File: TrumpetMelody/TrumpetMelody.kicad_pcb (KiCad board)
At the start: 2 copper layers, 76.2 x 68.6 mm, 81 parts, among them J1 USB_B_Micro, J2 Conn_01x05, J3 640456-3, J4 640456-3, SW1 SW_Push, U1 STM32F411RETx, U2 TLV62565DBVR, U3 MAX98357AETE_T, U4 MAX7375AXR805

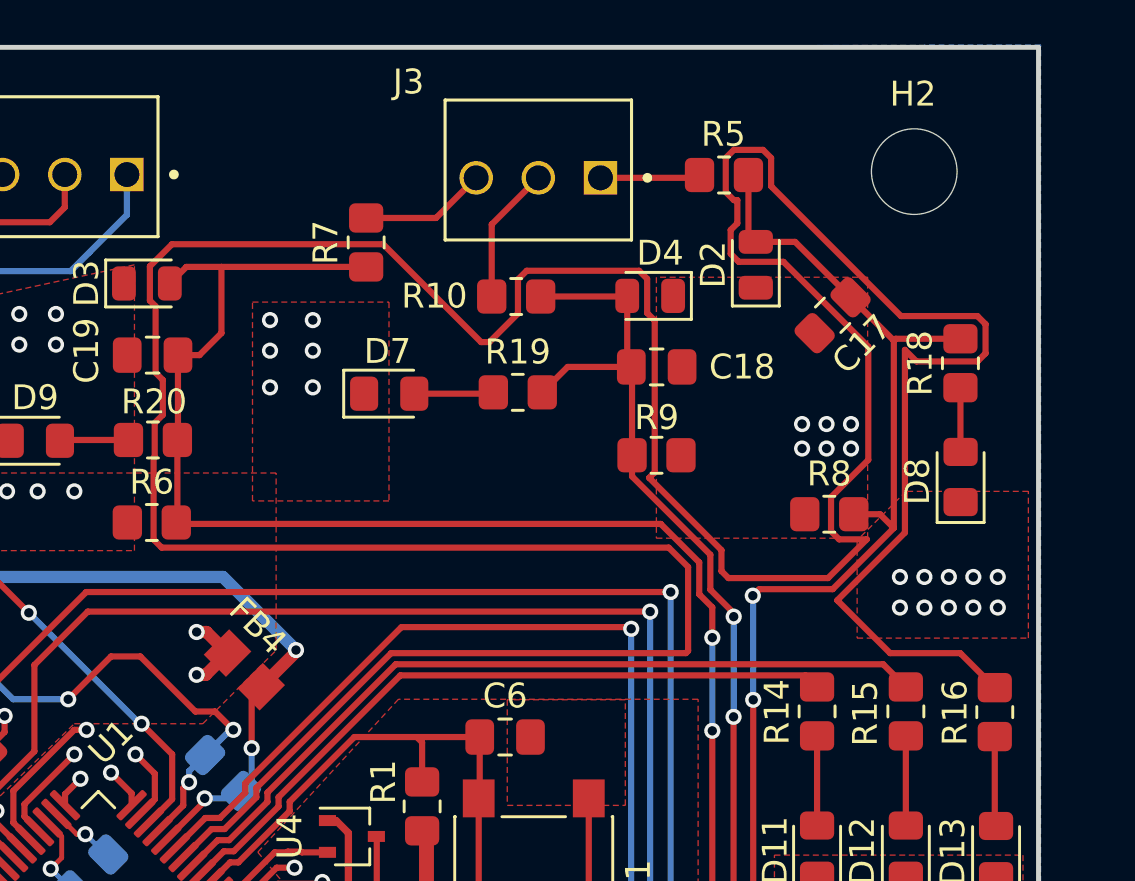
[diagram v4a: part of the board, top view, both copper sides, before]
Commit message: something autorouted and i just noticed it but now it is fixed
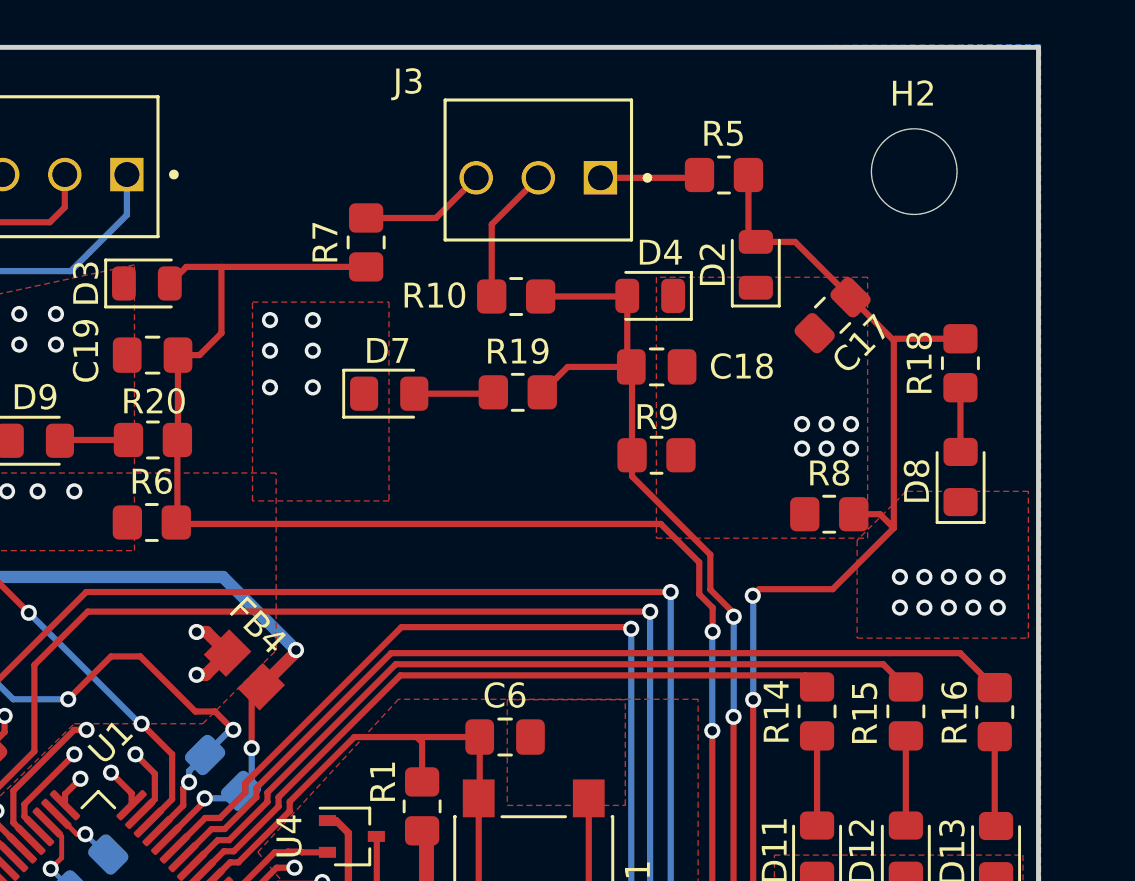
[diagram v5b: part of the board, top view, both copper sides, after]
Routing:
- net GPIO_LED2: track 166.0 -> 37.4 mm

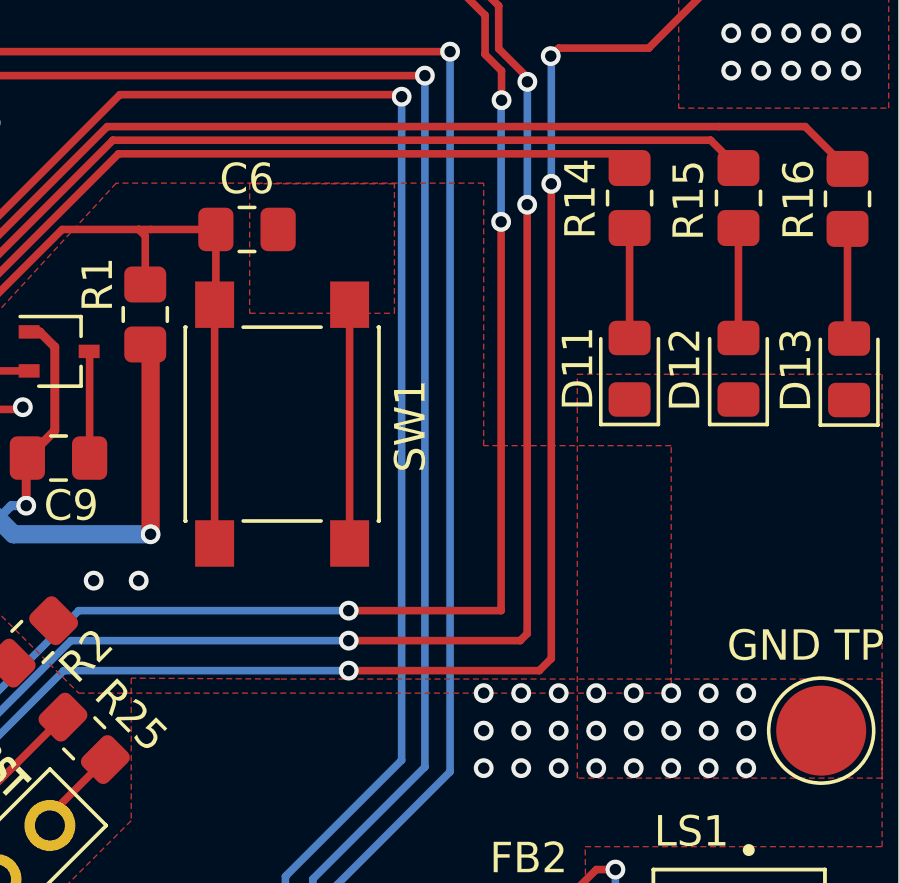
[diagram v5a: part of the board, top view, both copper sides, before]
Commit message: Fixed a right angle
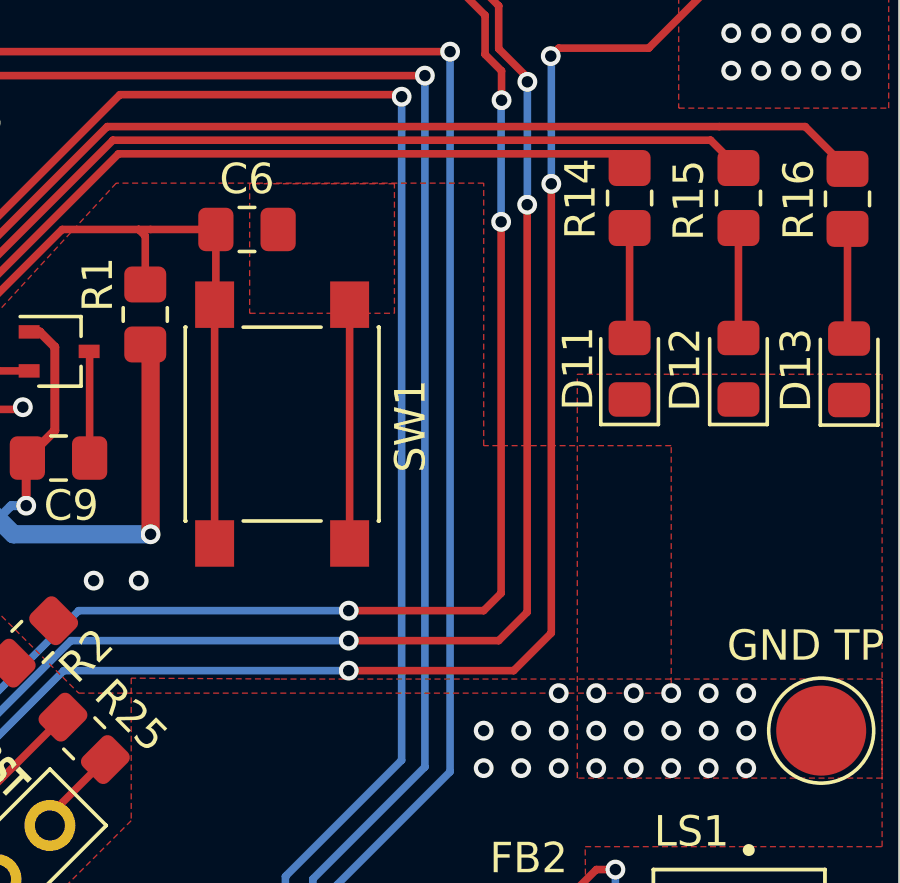
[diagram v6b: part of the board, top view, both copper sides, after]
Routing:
- net GND: vias 147 -> 145
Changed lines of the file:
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@@
   (via (at 174.605 72.87) (size 0.6604) (drill 0.381) (layers "F.Cu" "B.Cu") (free) (net 2))
   (via (at 178.725744 107.974565) (size 0.6604) (drill 0.381) (layers "F.Cu" "B.Cu") (free) (net 2))
-  (via (at 210.855 89.37) (size 0.6604) (drill 0.381) (layers "F.Cu" "B.Cu") (free) (net 2))
   (via (at 169.291 88.646) (size 0.6604) (drill 0.381) (layers "F.Cu" "B.Cu") (free) (net 2))
   (via (at 209.605 91.87) (size 0.6604) (drill 0.381) (layers "F.Cu" "B.Cu") (free) (net 2))
@@
   (via (at 202.105 103.62) (size 0.6604) (drill 0.381) (layers "F.Cu" "B.Cu") (free) (net 2))
   (via (at 164.465 78.994) (size 0.6604) (drill 0.381) (layers "F.Cu" "B.Cu") (free) (net 2))
-  (via (at 209.605 89.37) (size 0.6604) (drill 0.381) (layers "F.Cu" "B.Cu") (free) (net 2))
   (via (at 199.105 110.62) (size 0.6604) (drill 0.381) (layers "F.Cu" "B.Cu") (net 2))
   (via (at 198.105 85.62) (size 0.6604) (drill 0.381) (layers "F.Cu" "B.Cu") (free) (net 2))
@@
   (segment (start 179.075954 75.889246) (end 179.075954 76.067046) (width 0.254) (layer "F.Cu") (net 10))
   (segment (start 177.673 79.840588) (end 179.128608 81.296196) (width 0.254) (layer "F.Cu") (net 10))
+  (segment (start 211.857768 72.392265) (end 211.857768 87.367232) (width 0.254) (layer "F.Cu") (net 11))
   (segment (start 188.568611 91.23644) (end 188.568611 90.736199) (width 0.254) (layer "F.Cu") (net 11))
   (segment (start 212.105 67.87) (end 215.105 67.87) (width 0.254) (layer "F.Cu") (net 11))
-  (segment (start 211.857768 88.217232) (end 211.455 88.62) (width 0.254) (layer "F.Cu") (net 11))
   (segment (start 211.662118 50.938708) (end 211.662118 53.371618) (width 0.254) (layer "F.Cu") (net 11))
+  (segment (start 211.857768 87.367232) (end 210.605 88.62) (width 0.254) (layer "F.Cu") (net 11))
   (segment (start 217.605 57.706667) (end 215.836078 55.937745) (width 0.254) (layer "F.Cu") (net 11))
+  (segment (start 210.605 88.62) (end 205.105 88.62) (width 0.254) (layer "F.Cu") (net 11))
   (segment (start 188.568611 90.736199) (end 187.15427 89.321858) (width 0.254) (layer "F.Cu") (net 11))
   (segment (start 188.653585 91.321414) (end 188.568611 91.23644) (width 0.254) (layer "F.Cu") (net 11))
-  (segment (start 205.105 88.62) (end 211.455 88.62) (width 0.254) (layer "F.Cu") (net 11))
   (segment (start 215.105 67.87) (end 217.605 65.37) (width 0.254) (layer "F.Cu") (net 11))
   (segment (start 217.605 65.37) (end 217.040458 64.805458) (width 0.254) (layer "F.Cu") (net 11))
-  (segment (start 211.857768 72.392265) (end 211.857768 88.217232) (width 0.254) (layer "F.Cu") (net 11))
   (segment (start 211.662118 53.371618) (end 211.963 53.6725) (width 0.254) (layer "F.Cu") (net 11))
   (segment (start 217.040458 64.805458) (end 215.965738 64.805458) (width 0.254) (layer "F.Cu") (net 11))
@@
   (segment (start 203.168 55.9054) (end 206.6821 55.9054) (width 0.254) (layer "F.Cu") (net 12))
   (segment (start 189.225811 90.570706) (end 189.110226 90.570706) (width 0.254) (layer "F.Cu") (net 12))
+  (segment (start 210.105 87.62) (end 205.105 87.62) (width 0.254) (layer "F.Cu") (net 12))
   (segment (start 210.105 66.460948) (end 210.105 67.890948) (width 0.254) (layer "F.Cu") (net 12))
-  (segment (start 205.105 87.62) (end 210.82 87.62) (width 0.254) (layer "F.Cu") (net 12))
+  (segment (start 211.053703 86.671297) (end 210.105 87.62) (width 0.254) (layer "F.Cu") (net 12))
   (segment (start 206.904403 62.394663) (end 206.904403 58.814212) (width 0.254) (layer "F.Cu") (net 12))
-  (segment (start 211.053703 73.08801) (end 211.053703 87.386297) (width 0.254) (layer "F.Cu") (net 12))
+  (segment (start 211.053703 73.08801) (end 211.053703 86.671297) (width 0.254) (layer "F.Cu") (net 12))
   (segment (start 210.105 67.890948) (end 211.060276 68.846224) (width 0.254) (layer "F.Cu") (net 12))
   (segment (start 189.110226 90.570706) (end 187.507824 88.968304) (width 0.254) (layer "F.Cu") (net 12))
@@
   (segment (start 206.7075 55.88) (end 206.7075 58.617309) (width 0.254) (layer "F.Cu") (net 12))
   (segment (start 206.6821 55.9054) (end 206.7075 55.88) (width 0.254) (layer "F.Cu") (net 12))
-  (segment (start 211.053703 87.386297) (end 210.82 87.62) (width 0.254) (layer "F.Cu") (net 12))
   (segment (start 206.874152 58.783961) (end 204.273075 58.783961) (width 0.254) (layer "F.Cu") (net 12))
   (segment (start 211.060276 68.846224) (end 211.060276 68.992484) (width 0.254) (layer "F.Cu") (net 12))
@@
   (segment (start 188.318041 65.098172) (end 188.272737 65.143476) (width 0.254) (layer "F.Cu") (net 13))
   (segment (start 188.34206 58.301493) (end 188.34206 61.7462) (width 0.254) (layer "F.Cu") (net 13))
+  (segment (start 210.185 86.04) (end 210.185 73.66) (width 0.254) (layer "F.Cu") (net 13))
   (segment (start 188.34206 61.7462) (end 188.318041 61.770219) (width 0.254) (layer "F.Cu") (net 13))
   (segment (start 188.87017 89.623544) (end 187.861377 88.614751) (width 0.254) (layer "F.Cu") (net 13))
-  (segment (start 205.105 86.62) (end 210.185 86.62) (width 0.254) (layer "F.Cu") (net 13))
   (segment (start 209.651 68.079) (end 209.651 66.775644) (width 0.254) (layer "F.Cu") (net 13))
-  (segment (start 210.185 86.62) (end 210.185 73.66) (width 0.254) (layer "F.Cu") (net 13))
   (segment (start 188.34206 58.301493) (end 189.221507 58.301493) (width 0.254) (layer "F.Cu") (net 13))
   (segment (start 188.68528 54.69522) (end 188.0085 55.372) (width 0.254) (layer "F.Cu") (net 13))
   (segment (start 196.035339 54.69522) (end 190.119 54.69522) (width 0.254) (layer "F.Cu") (net 13))
+  (segment (start 209.605 86.62) (end 210.185 86.04) (width 0.254) (layer "F.Cu") (net 13))
   (segment (start 190.119 54.69522) (end 188.68528 54.69522) (width 0.254) (layer "F.Cu") (net 13))
   (segment (start 190.119 57.404) (end 190.119 54.69522) (width 0.254) (layer "F.Cu") (net 13))
@@
   (segment (start 188.318041 61.770219) (end 188.318041 65.098172) (width 0.254) (layer "F.Cu") (net 13))
   (segment (start 209.651 66.775644) (end 208.077156 65.2018) (width 0.254) (layer "F.Cu") (net 13))
+  (segment (start 205.105 86.62) (end 209.605 86.62) (width 0.254) (layer "F.Cu") (net 13))
   (via (at 210.199926 69.606315) (size 0.6604) (drill 0.381) (layers "F.Cu" "B.Cu") (free) (net 13))
   (via (at 189.235476 89.623544) (size 0.6604) (drill 0.381) (layers "F.Cu" "B.Cu") (free) (net 13))

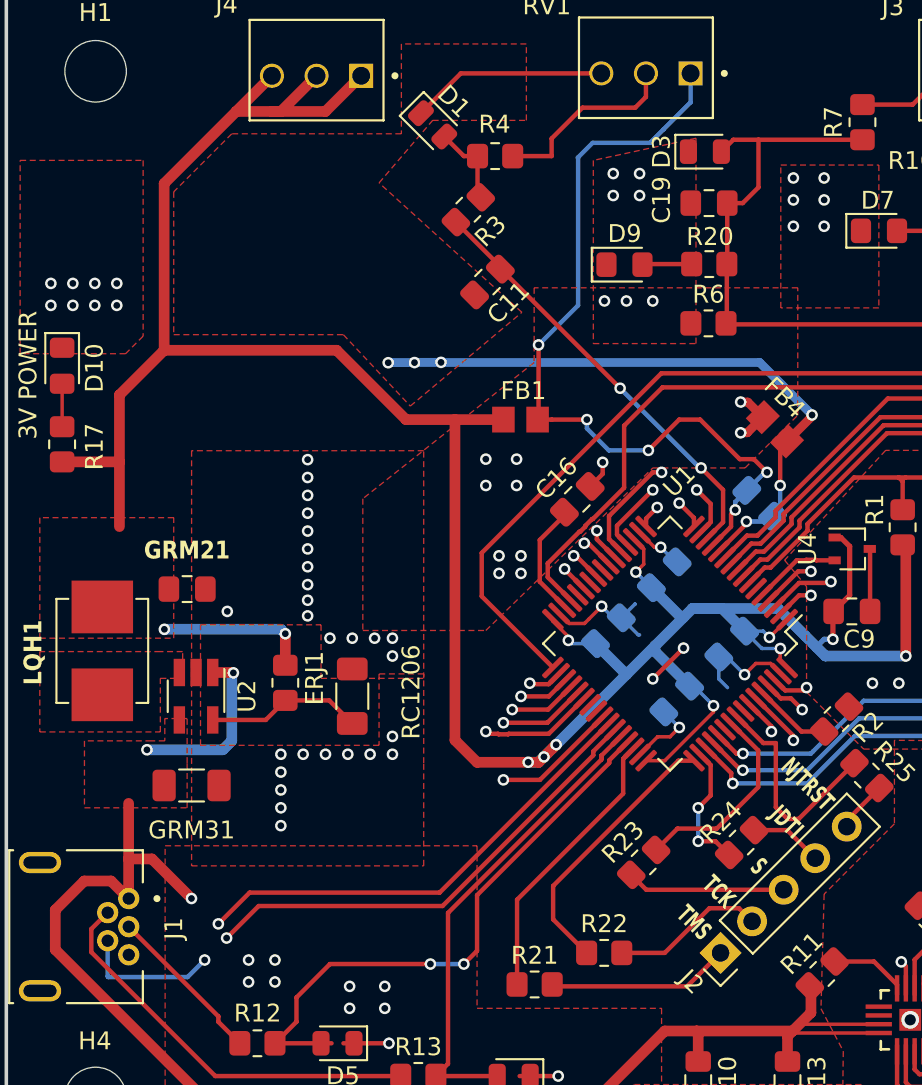
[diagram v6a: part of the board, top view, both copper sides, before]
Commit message: changed some traces
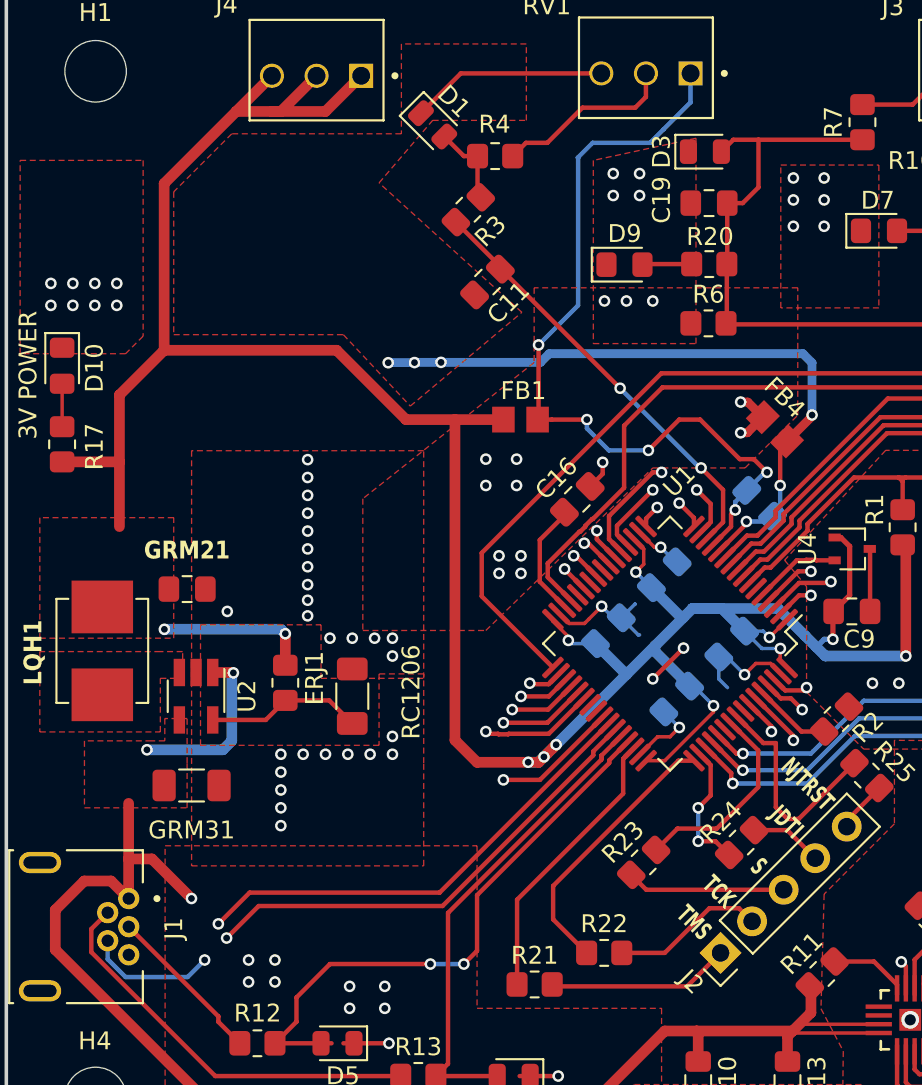
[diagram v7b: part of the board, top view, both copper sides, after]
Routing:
- net GNDA: track 47.2 -> 49.4 mm
- net Net-(R4-Pad2): track 10.9 -> 10.3 mm
- net USB_ID_Connector: track 7.97 -> 7.39 mm
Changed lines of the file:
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@@
   (via (at 169.049353 67.383846) (size 0.6604) (drill 0.381) (layers "F.Cu" "B.Cu") (net 4))
   (via (at 172.054488 67.362739) (size 0.6604) (drill 0.381) (layers "F.Cu" "B.Cu") (net 4))
-  (segment (start 190.179 67.37) (end 193.167 70.358) (width 0.5) (layer "B.Cu") (net 4))
+  (segment (start 177.715631 67.362739) (end 178.20837 66.87) (width 0.5) (layer "B.Cu") (net 4))
   (segment (start 170.558718 67.362739) (end 170.545712 67.375745) (width 0.254) (layer "B.Cu") (net 4))
+  (segment (start 192.647803 66.87) (end 193.167 67.389197) (width 0.5) (layer "B.Cu") (net 4))
   (segment (start 172.054488 67.362739) (end 170.558718 67.362739) (width 0.5) (layer "B.Cu") (net 4))
   (segment (start 189.434147 76.419941) (end 190.616312 76.419941) (width 0.254) (layer "B.Cu") (net 4))
@@
   (segment (start 169.057454 67.375745) (end 169.049353 67.383846) (width 0.254) (layer "B.Cu") (net 4))
   (segment (start 191.355 75.681253) (end 190.919614 76.116639) (width 0.254) (layer "B.Cu") (net 4))
-  (segment (start 172.061749 67.37) (end 172.054488 67.362739) (width 0.5) (layer "B.Cu") (net 4))
-  (segment (start 190.179 67.37) (end 172.061749 67.37) (width 0.5) (layer "B.Cu") (net 4))
+  (segment (start 193.167 67.389197) (end 193.167 70.358) (width 0.5) (layer "B.Cu") (net 4))
+  (segment (start 172.054488 67.362739) (end 177.715631 67.362739) (width 0.5) (layer "B.Cu") (net 4))
   (segment (start 191.355 74.37) (end 191.355 75.681253) (width 0.254) (layer "B.Cu") (net 4))
+  (segment (start 178.20837 66.87) (end 192.647803 66.87) (width 0.5) (layer "B.Cu") (net 4))
   (segment (start 172.041482 67.375745) (end 172.054488 67.362739) (width 0.254) (layer "B.Cu") (net 4))
   (segment (start 170.545712 67.375745) (end 169.057454 67.375745) (width 0.5) (layer "B.Cu") (net 4))
@@
   (segment (start 159.385 104.888769) (end 160.605925 106.109694) (width 0.254) (layer "F.Cu") (net 28))
   (via (at 158.605 101.37) (size 0.6604) (drill 0.381) (layers "F.Cu" "B.Cu") (net 29))
-  (segment (start 153.086352 102.307455) (end 153.086352 100.274978) (width 0.254) (layer "B.Cu") (net 29))
-  (segment (start 153.120011 102.341114) (end 153.086352 102.307455) (width 0.254) (layer "B.Cu") (net 29))
-  (segment (start 157.633886 102.341114) (end 153.120011 102.341114) (width 0.254) (layer "B.Cu") (net 29))
   (segment (start 158.605 101.37) (end 157.633886 102.341114) (width 0.254) (layer "B.Cu") (net 29))
+  (segment (start 153.086352 101.322466) (end 153.086352 100.274978) (width 0.254) (layer "B.Cu") (net 29))
+  (segment (start 157.633886 102.341114) (end 154.105 102.341114) (width 0.254) (layer "B.Cu") (net 29))
+  (segment (start 154.105 102.341114) (end 153.086352 101.322466) (width 0.254) (layer "B.Cu") (net 29))
   (segment (start 178.489977 102.87) (end 186.055 102.87) (width 0.254) (layer "F.Cu") (net 30))
   (segment (start 186.055 102.87) (end 187.96 100.965) (width 0.254) (layer "F.Cu") (net 30))
@@
   (segment (start 190.336251 86.139877) (end 192.566374 88.37) (width 0.254) (layer "F.Cu") (net 39))
   (segment (start 192.566374 88.37) (end 193.855 88.37) (width 0.254) (layer "F.Cu") (net 39))
-  (segment (start 178.349 54.626) (end 178.349 55.626) (width 0.254) (layer "F.Cu") (net 40))
-  (segment (start 180.105 52.87) (end 178.349 54.626) (width 0.254) (layer "F.Cu") (net 40))
-  (segment (start 176.133 55.626) (end 178.349 55.626) (width 0.254) (layer "F.Cu") (net 40))
   (segment (start 183.715606 50.919442) (end 183.715606 52.259394) (width 0.254) (layer "F.Cu") (net 40))
+  (segment (start 176.889 54.87) (end 176.133 55.626) (width 0.254) (layer "F.Cu") (net 40))
   (segment (start 183.105 52.87) (end 180.105 52.87) (width 0.254) (layer "F.Cu") (net 40))
+  (segment (start 180.105 52.87) (end 178.105 54.87) (width 0.254) (layer "F.Cu") (net 40))
+  (segment (start 178.105 54.87) (end 176.889 54.87) (width 0.254) (layer "F.Cu") (net 40))
   (segment (start 183.715606 52.259394) (end 183.105 52.87) (width 0.254) (layer "F.Cu") (net 40))
   (segment (start 198.005 102.77) (end 198.005 103.34) (width 0.254) (layer "F.Cu") (net 41))
